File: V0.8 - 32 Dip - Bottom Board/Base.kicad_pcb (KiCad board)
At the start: 4 copper layers, 18.5 x 41.7 mm, 17 parts, among them J1 Conn_01x20_Socket, J2 Conn_01x20_Socket, J4 Conn_01x16_Pin, J5 Conn_01x16_Pin, U1 74CBTD3861, U2 74LVC1G332, U3 MC74VHC1GT125, U5 74CBTD3861, U6 74CBTD3861, U7 74VHCT245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

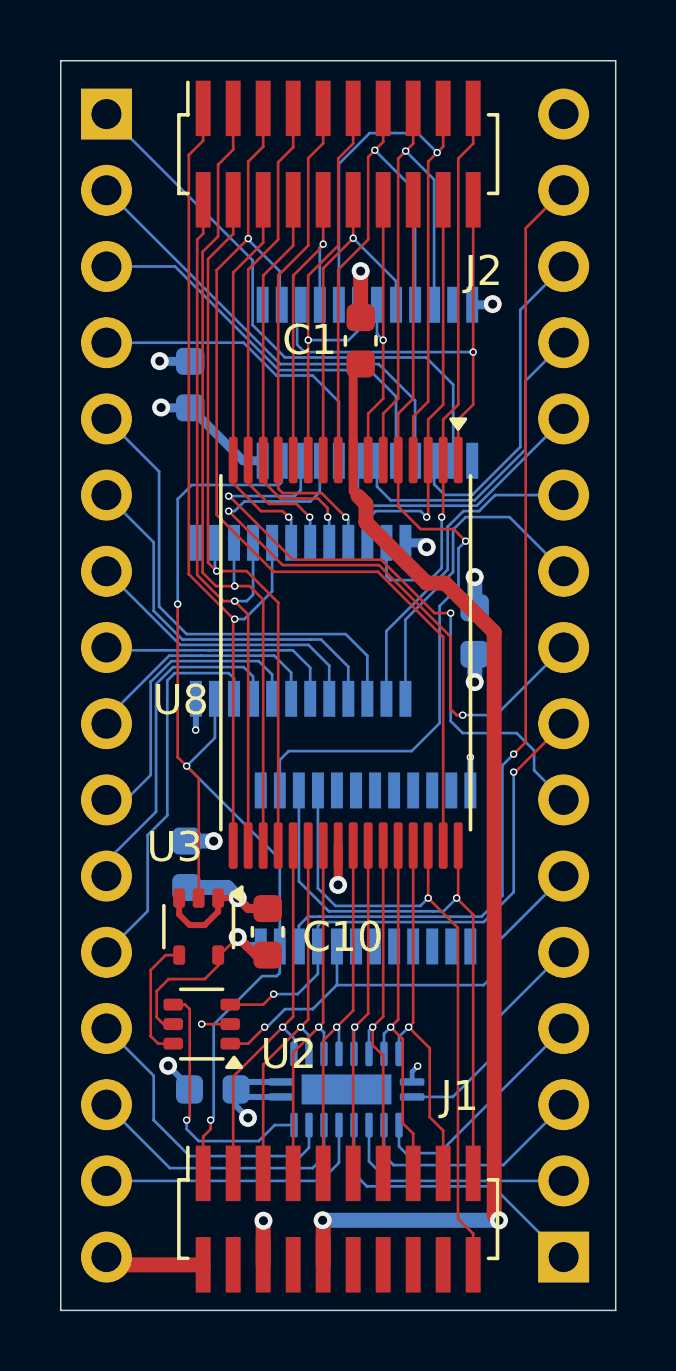
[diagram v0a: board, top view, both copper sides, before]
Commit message: added mounting holes to 0.1 headers
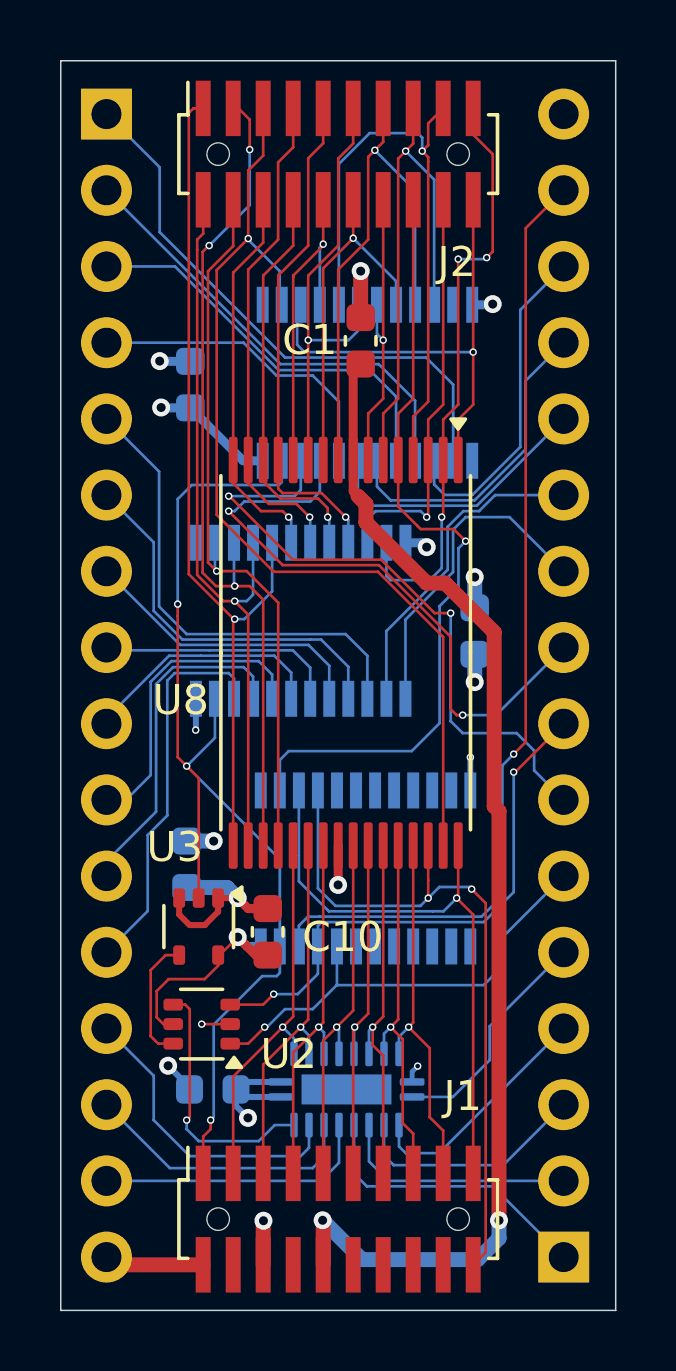
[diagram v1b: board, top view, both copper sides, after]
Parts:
- J1, J2: footprint Connector_PinSocket_1.00mm:PinSocket_2x10_P1.00mm_Vertical_SMD -> JJGTechnologies_Footprint_Library:PinSocket_2x10_P1.00mm_Vertical_SMD
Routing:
- net /~{3v3-CE}: track 21.9 -> 23.6 mm, vias 1 -> 2
- net /3v3: track 38.4 -> 39.8 mm
- net /3v3-A9: track 19.1 -> 20.0 mm, vias 1 -> 3
- net /3v3-A1: track 27.9 -> 28.5 mm, vias 1 -> 3

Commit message: Logic OR fix
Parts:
- added R1: 20k, Resistor_SMD:R_0402_1005Metric, B.Cu at (147.7, 111.2)
- U2: value 74LVC1G332 -> 74AHC1G32; footprint Package_TO_SOT_SMD:SOT-363_SC-70-6 -> Package_TO_SOT_SMD:SOT-353_SC-70-5
- moved U2 0.22 mm to (147.8, 113.7)
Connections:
- U2 pad 2: /GND -> /~{OE}
- U2 pad 3: /~{OE} -> /5v
- U2 pad 4: Net-(U2-Y) -> Net-(U2-Pad4)
- U2 pad 5: /5v -> /GND
- U3 pad 1: /GND -> /~{3v3-BusConnect}
- U3 pad 2: /~{3v3-BusConnect} -> Net-(U2-Pad4)
- U3 pad 4: Net-(U2-A) -> Net-(U7-CE)
- U7 pad 19: Net-(U2-Y) -> Net-(U7-CE)
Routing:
- net Net-(U7-CE): track 0.00 -> 10.7 mm, vias 0 -> 2
- net Net-(U2-Y): track 8.62 -> 0.00 mm, vias 1 -> 0
- net Net-(U2-Pad4): track 0.00 -> 4.24 mm
- net Net-(U2-A): track 4.21 -> 0.00 mm
- net /GND: track 20.1 -> 18.5 mm
- net /5v: track 20.1 -> 19.1 mm
- net unconnected-(J1-Pin_4-Pad4): track 0.00 -> 0.77 mm

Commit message: Removed Buffer updated Or logic.
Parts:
- removed U3: MC74VHC1GT125, Package_TO_SOT_SMD:SOT-353_SC-70-5
- added R2: 0ohm, Resistor_SMD:R_0402_1005Metric, B.Cu at (148.1, 114.3)
- added R3: DNP, Resistor_SMD:R_0402_1005Metric, B.Cu at (148.1, 113.4)
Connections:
- R1 pad 1: Net-(U7-CE) -> Net-(U1-A4)
- U1 pad 19: unconnected-(U1-B4-Pad19) -> Net-(U1-B4)
- U1 pad 5: unconnected-(U1-A4-Pad5) -> Net-(U1-A4)
- U2 pad 1: /~{CE} -> Net-(R2-Pad1)
- U2 pad 4: Net-(U2-Pad4) -> Net-(U1-B4)
- U7 pad 19: Net-(U7-CE) -> Net-(U1-A4)
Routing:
- net Net-(U1-A4): track 0.00 -> 24.5 mm
- net Net-(U7-CE): track 10.7 -> 0.00 mm, vias 2 -> 0
- net Net-(U1-B4): track 0.00 -> 7.43 mm, vias 0 -> 1
- net Net-(U2-Pad4): track 4.24 -> 0.00 mm
- net /~{3v3-BusConnect}: track 37.5 -> 33.7 mm
- net Net-(R2-Pad1): track 0.00 -> 3.11 mm, vias 0 -> 1
- net /~{3v3-CE}: track 23.6 -> 22.4 mm
- net /~{CE}: track 15.5 -> 16.7 mm, vias 1 -> 2
- net /~{3v3-OE}: track 20.1 -> 19.0 mm
- net /5v: track 19.1 -> 18.2 mm
- net /GND: track 18.5 -> 17.9 mm
- net /~{3v3-FL_WE}: vias 1 -> 3

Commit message: Add Probe PCB, Latest Top/Bottom PCBs
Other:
- board text added: "Flying Rommy V0.8 Bottom PCB"
- board text removed: "Flying Rommy V0.8"
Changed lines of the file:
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@@
 		(tags "resistor")
 		(property "Reference" "R3"
-			(at -1.15 6.6 360)
+			(at -1.15 6.6 0)
 			(layer "B.SilkS")
 			(effects
@@
 		)
 		(property "Value" "DNP"
-			(at 0 -1.17 360)
+			(at 0 -1.17 0)
 			(layer "B.Fab")
 			(effects
@@
 		)
 		(fp_text user "${REFERENCE}"
-			(at 0 0 360)
+			(at 0 0 0)
 			(layer "B.Fab")
 			(effects
@@
 		(tags "resistor")
 		(property "Reference" "R2"
-			(at -1.1 7 360)
+			(at -1.1 7 0)
 			(layer "B.SilkS")
 			(effects
@@
 		)
 		(property "Value" "0ohm"
-			(at 0 -1.17 360)
+			(at 0 -1.17 0)
 			(layer "B.Fab")
 			(effects
@@
 		)
 		(fp_text user "${REFERENCE}"
-			(at 0 0 360)
+			(at 0 0 0)
 			(layer "B.Fab")
 			(effects
@@
 		(tags "capacitor")
 		(property "Reference" "C5"
-			(at -2.072 0.043 360)
+			(at -2.072 0.043 0)
 			(layer "B.SilkS")
 			(effects
@@
 		(layer "Edge.Cuts")
 	)
-	(gr_text "Flying Rommy\n    V0.8"
-		(at 155.930915 84.423766 0)
+	(gr_text "Flying Rommy\nV0.8\nBottom PCB"
+		(at 152.2 85.5 0)
 		(layer "B.SilkS")
 		(effects
@@
 				(bold yes)
 			)
-			(justify left bottom mirror)
+			(justify bottom mirror)
 		)
 	)
 	(gr_text "JJG Technologies \n    ©2025"
-		(at 157.226 87.5792 0)
+		(at 157.4 88.4 0)
 		(layer "B.SilkS")
 		(effects
